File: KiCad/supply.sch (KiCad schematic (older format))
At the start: 74 parts, among them IC10 AP62301Z6-7, IC12 74HC00PW, IC13 SN74LVC1G126DCKR, IC3 TPS54561, IC4 TPS7A0518PDBVT, IC8 LM3671MF-3.3, IC9 LM3671MF-3.3, T3 BSS138APW

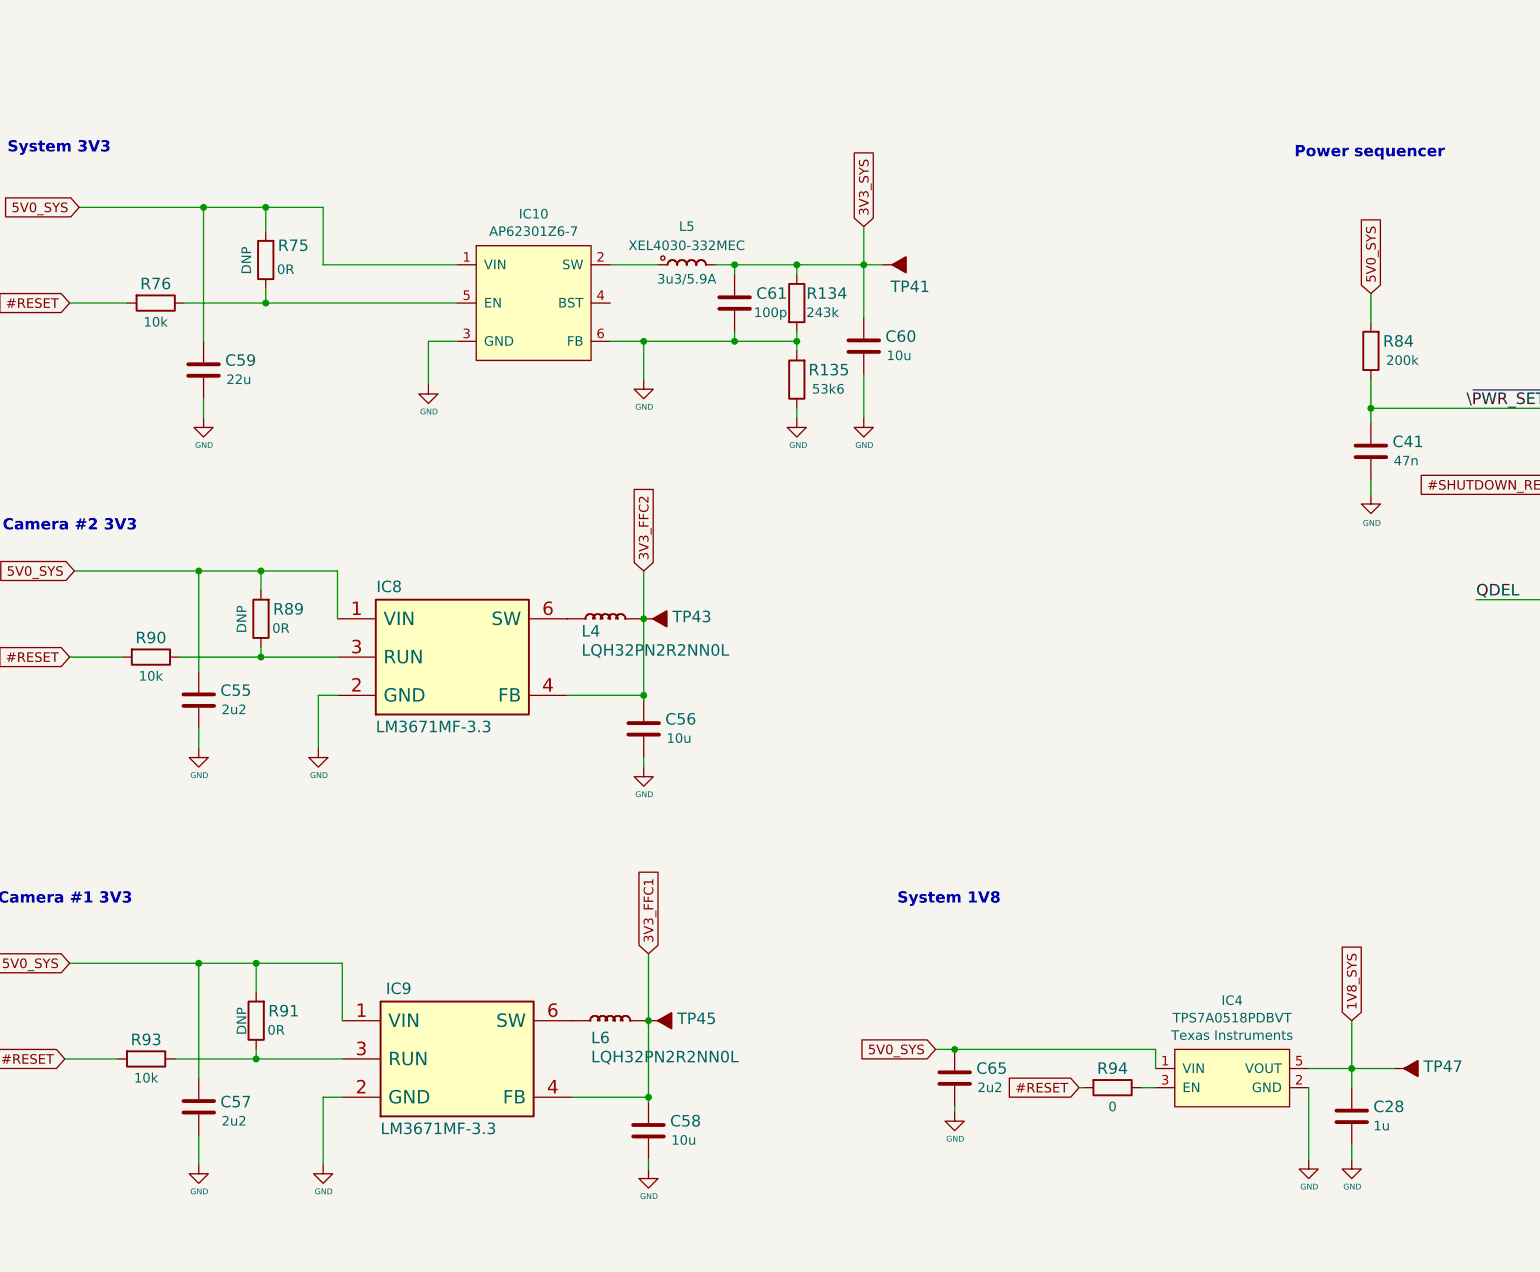
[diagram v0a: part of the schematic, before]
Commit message: DCDC passives copied
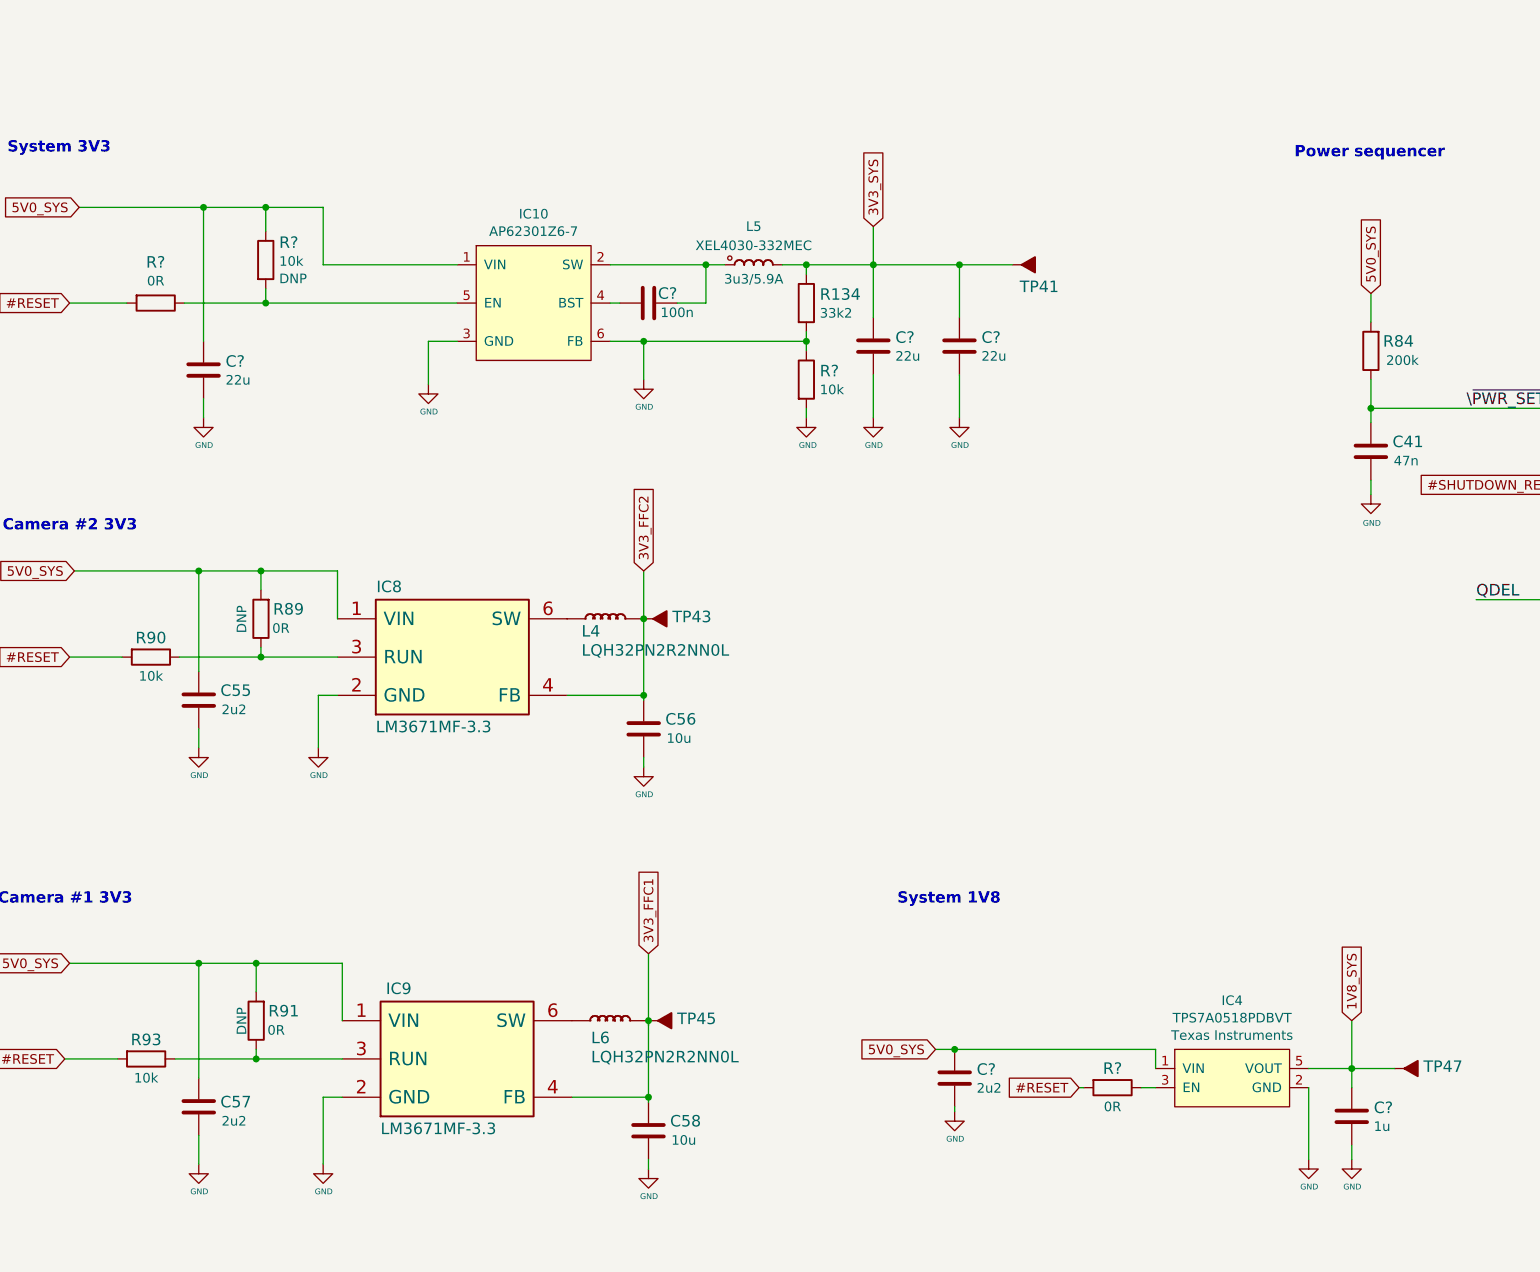
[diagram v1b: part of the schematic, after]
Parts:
- removed C28: C_1u_0402, jetson-nano-baseboard-footprints:0402-cap, symbol jetson-nano-baseboard:C_1u_0402
- removed C59: C_22u_0603, jetson-nano-baseboard-footprints:0603-cap, symbol jetson-nano-baseboard:C_2u2_0402
- removed C60: C_10u_0603, jetson-nano-baseboard-footprints:0603-cap, symbol jetson-nano-baseboard:C_10u_0603
- removed C61: C_100n_0402, jetson-nano-baseboard-footprints:0402-cap, symbol jetson-nano-baseboard:C_100p_0402
- removed C65: C_2u2_0402, jetson-nano-baseboard-footprints:0402-cap, symbol jetson-nano-baseboard:C_2u2_0402
- removed R134: R_243k_0402, jetson-nano-baseboard-footprints:0402-res, symbol jetson-nano-baseboard:R_243k_0402
- removed R135: R_53k6_0402, jetson-nano-baseboard-footprints:0402-res, symbol jetson-nano-baseboard:R_53k6_0402
- removed R75: R_10k_0402, jetson-nano-baseboard-footprints:0402-res, symbol jetson-nano-baseboard:R_0R_0402
- removed R76, R94: R_0R_0402, jetson-nano-baseboard-footprints:0402-res, symbol jetson-nano-baseboard:R_10k_0402
- added C? (x3): C_22u_0603, antmicro-footprints:0603-cap, symbol antmicroCapacitors0603:C_22u_0603
- added C?: C_100n_0402, antmicro-footprints:0402-cap, symbol antmicroCapacitors0402:C_100n_0402
- added C?: C_2u2_0402, antmicro-footprints:0402-cap, symbol antmicroCapacitors0402:C_2u2_0402
- added C?: C_1u_0402, antmicro-footprints:0402-cap, symbol antmicroCapacitors0402:C_1u_0402
- added R134: R_33k2_0402, antmicro-footprints:0402-res, symbol antmicroResistors0402:R_33k2_0402
- added R? (x2): R_10k_0402, antmicro-footprints:0402-res, symbol antmicroResistors0402:R_10k_0402
- added R? (x2): R_0R_0402, antmicro-footprints:0402-res, symbol antmicroResistors0402:R_0R_0402
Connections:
- net #RESET: now also R?.2, R?.2
- net 1V8_SYS: now also C?.1
- net 3V3_SYS: now also C?.1, C?.1, R134.1
- net 5V0_SYS: now also C?.1, C?.1, R?.1
- net GND: now also C?.2, C?.2, C?.2, C?.2, C?.2, R134.2, R?.1, R?.2
- net at IC4.3 (EN): now also R?.1
- net at IC10.2 (SW), L5.1 (P): now also C?.1
- net at IC10.4 (BST): now also C?.2
- net at IC10.5 (EN): now also R?.1, R?.2
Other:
- moved on the sheet: L5, TP41

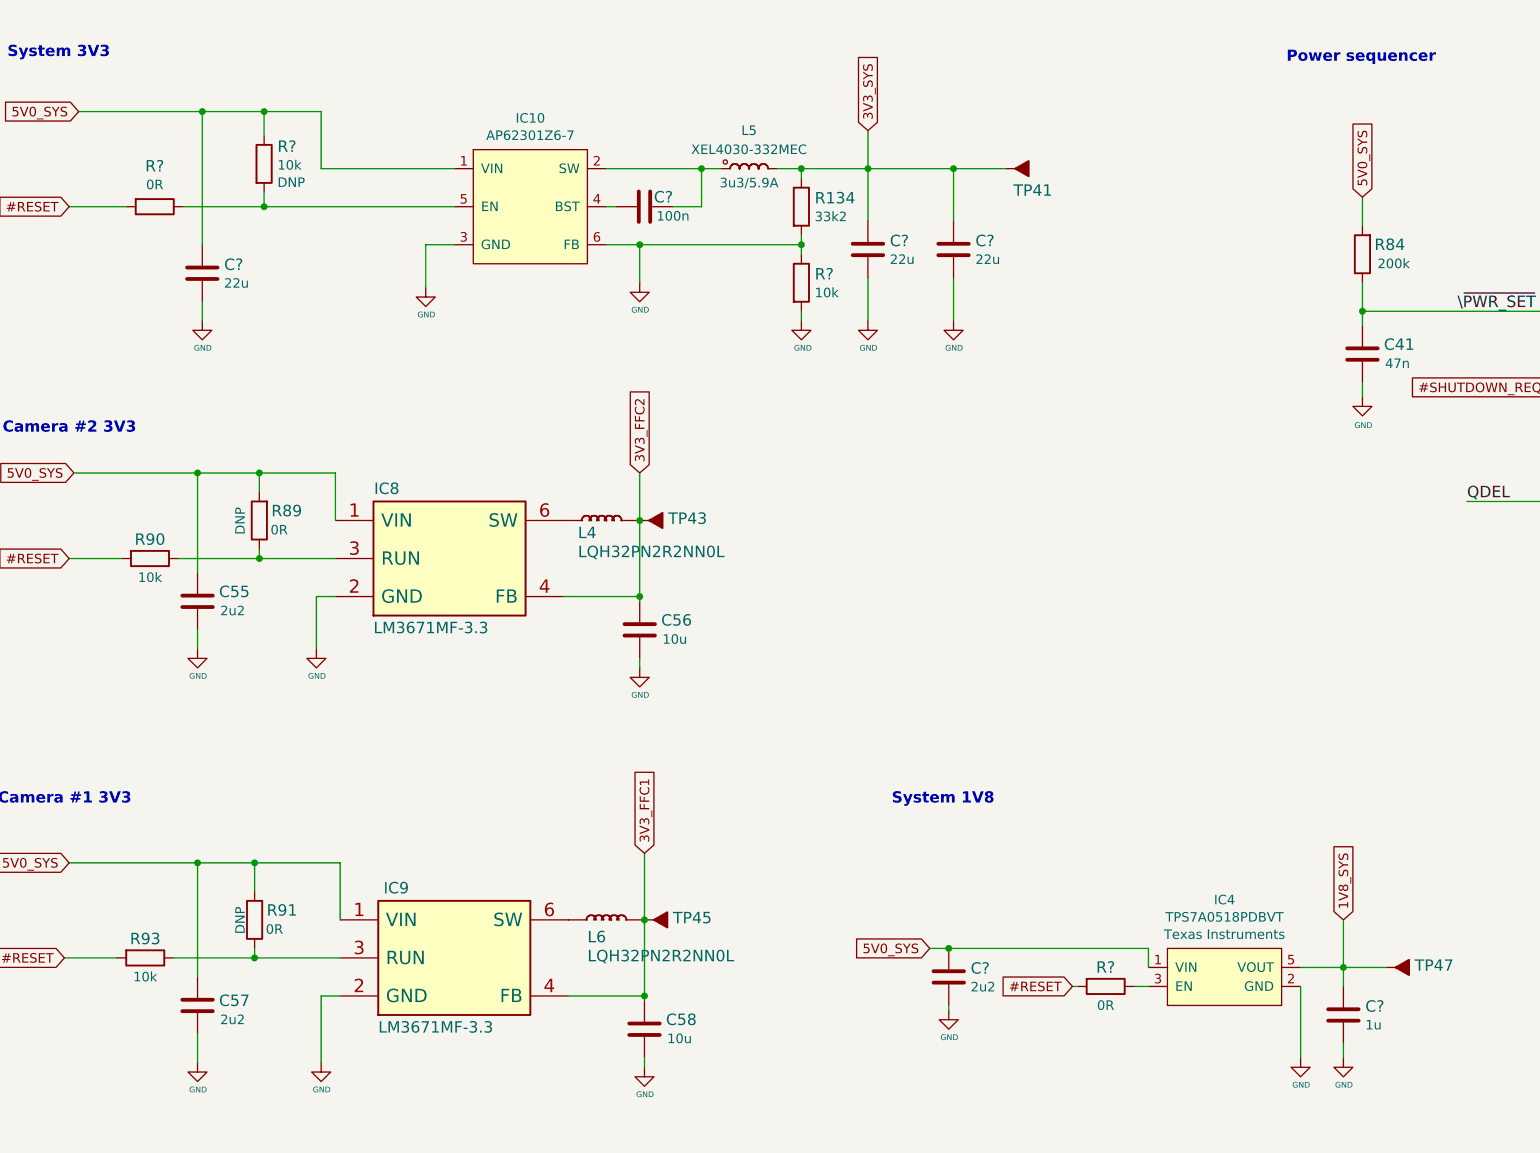
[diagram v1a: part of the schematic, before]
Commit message: Clean artefaccs, clean space for new DCDC
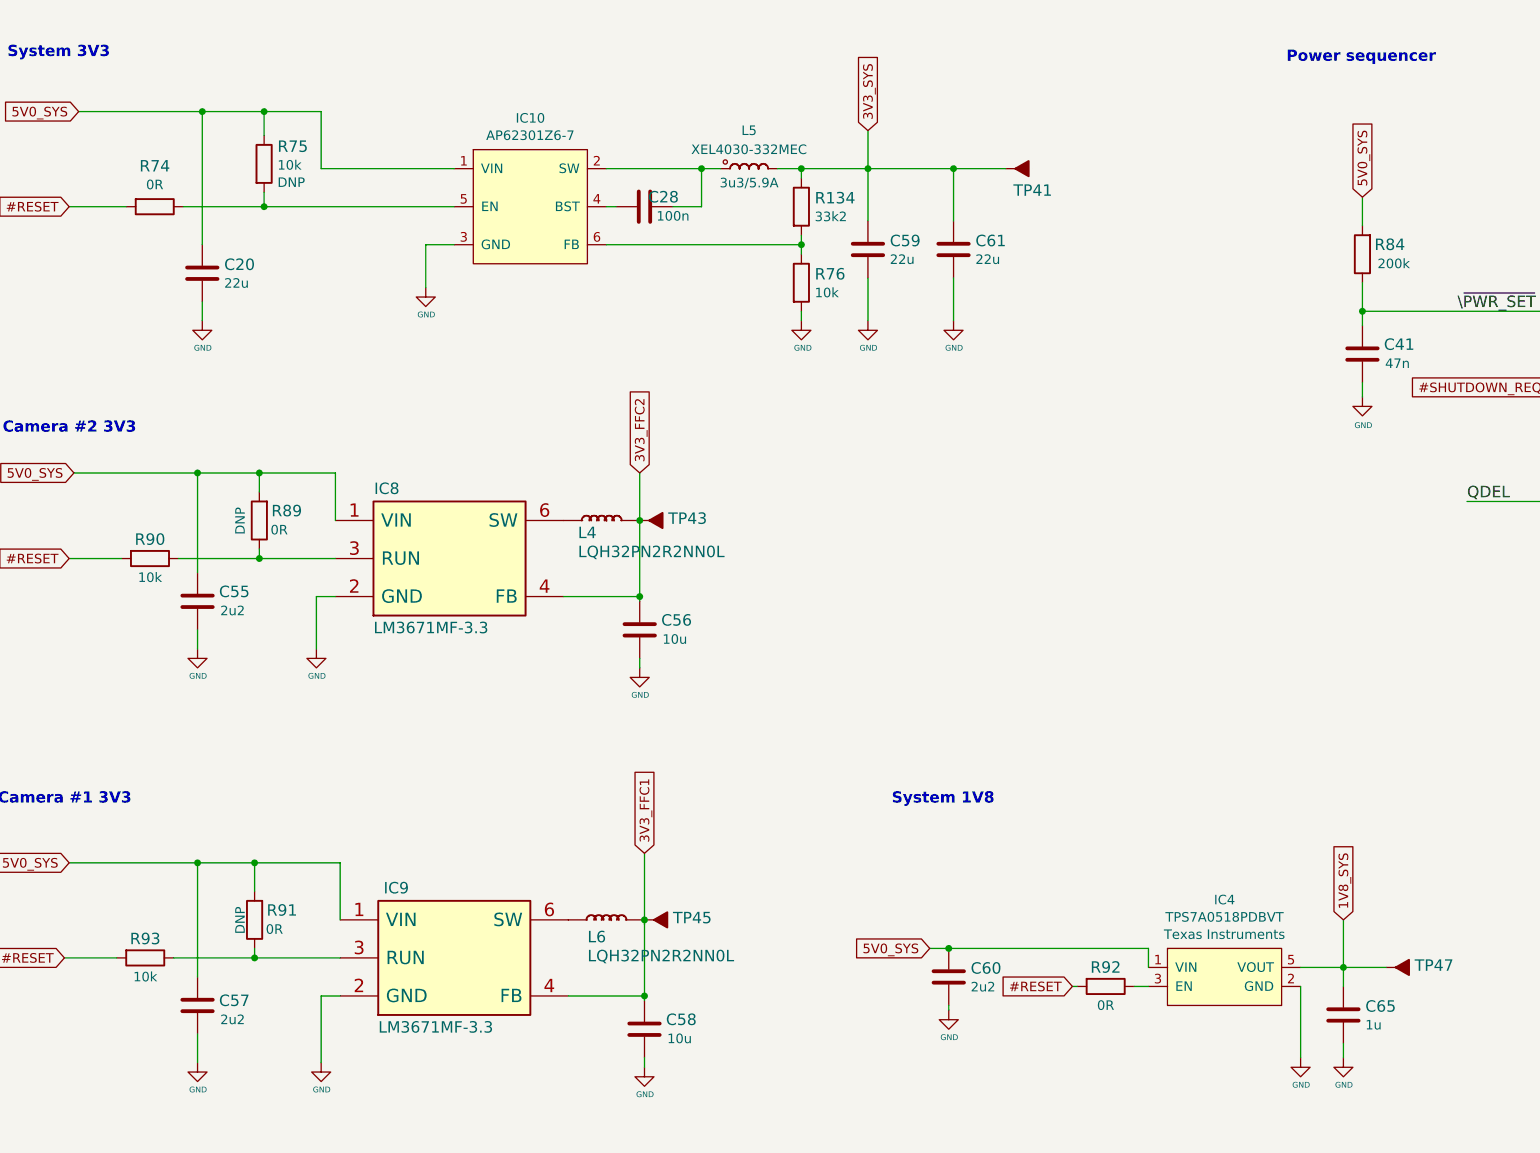
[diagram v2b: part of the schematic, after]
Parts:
- gave numbers to parts that had none: 10
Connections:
- net GND: no longer IC10.6 (FB), R134.2, R76.1
- new net: IC10.6 (FB), R134.2, R76.1
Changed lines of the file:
@@
-$EndComp
-$Comp
-L jetson-nano-baseboard:GND #GND_083
-U 1 1 5E7103BE
-P 4675 5900
-F 0 "#GND_083" H 4675 5900 20  0001 C CNN
-F 1 "GND" H 4678 5757 30  0000 C CNN
-F 2 "" H 4675 5900 70  0001 C CNN
-F 3 "" H 4675 5900 70  0001 C CNN
-	1    4675 5900
-	1    0    0    -1
 $EndComp
 $Comp
@@
 Wire Wire Line
 	3550 5700 3550 5925
-Wire Wire Line
-	4500 5700 4675 5700
-Wire Wire Line
-	4675 5700 4675 5900
 Wire Wire Line
 	1700 6900 2350 6900
@@
 $EndComp
 $Comp
-L antmicroResistors0402:R_10k_0402 R?
+L antmicroResistors0402:R_10k_0402 R76
 U 1 1 61619A9D
 P 5525 5900
-F 0 "R?" V 5480 5970 60  0000 L CNN
+F 0 "R76" V 5480 5970 60  0000 L CNN
 F 1 "R_10k_0402" H 5525 5750 60  0001 C CNN
 F 2 "antmicro-footprints:0402-res" H 5725 6100 60  0001 L CNN
@@
 $EndComp
 $Comp
-L antmicroCapacitors0603:C_22u_0603 C?
+L antmicroCapacitors0603:C_22u_0603 C59
 U 1 1 6162D00E
 P 5875 5725
-F 0 "C?" H 5990 5770 60  0000 L CNN
+F 0 "C59" H 5990 5770 60  0000 L CNN
 F 1 "C_22u_0603" H 5875 5575 60  0001 C CNN
 F 2 "antmicro-footprints:0603-cap" H 6075 5925 60  0001 L CNN
@@
 $EndComp
 $Comp
-L antmicroCapacitors0603:C_22u_0603 C?
+L antmicroCapacitors0603:C_22u_0603 C61
 U 1 1 61630270
 P 6325 5725
-F 0 "C?" H 6440 5770 60  0000 L CNN
+F 0 "C61" H 6440 5770 60  0000 L CNN
 F 1 "C_22u_0603" H 6325 5575 60  0001 C CNN
 F 2 "antmicro-footprints:0603-cap" H 6525 5925 60  0001 L CNN
@@
 $EndComp
 $Comp
-L antmicroCapacitors0402:C_100n_0402 C?
+L antmicroCapacitors0402:C_100n_0402 C28
 U 1 1 61632F02
 P 4700 5500
-F 0 "C?" V 4650 5600 60  0000 C CNN
+F 0 "C28" V 4650 5600 60  0000 C CNN
 F 1 "C_100n_0402" H 4700 5350 60  0001 C CNN
 F 2 "antmicro-footprints:0402-cap" H 4900 5700 60  0001 L CNN
@@
 $EndComp
 $Comp
-L antmicroResistors0402:R_0R_0402 R?
+L antmicroResistors0402:R_0R_0402 R74
 U 1 1 616348AD
 P 2125 5500
-F 0 "R?" H 2125 5287 60  0000 C CNN
+F 0 "R74" H 2125 5287 60  0000 C CNN
 F 1 "R_0R_0402" H 2125 5350 60  0001 C CNN
 F 2 "antmicro-footprints:0402-res" H 2325 5700 60  0001 L CNN
@@
 $EndComp
 $Comp
-L antmicroResistors0402:R_10k_0402 R?
+L antmicroResistors0402:R_10k_0402 R75
 U 1 1 61637618
 P 2700 5275
-F 0 "R?" V 2609 5345 60  0000 L CNN
+F 0 "R75" V 2609 5345 60  0000 L CNN
 F 1 "R_10k_0402" H 2700 5125 60  0001 C CNN
 F 2 "antmicro-footprints:0402-res" H 2900 5475 60  0001 L CNN
@@
 $EndComp
 $Comp
-L antmicroCapacitors0603:C_22u_0603 C?
+L antmicroCapacitors0603:C_22u_0603 C20
 U 1 1 6164BD87
 P 2375 5850
-F 0 "C?" H 2490 5895 60  0000 L CNN
+F 0 "C20" H 2490 5895 60  0000 L CNN
 F 1 "C_22u_0603" H 2375 5700 60  0001 C CNN
 F 2 "antmicro-footprints:0603-cap" H 2575 6050 60  0001 L CNN
@@
 	6325 5875 6325 6100
 $Comp
-L jetson-nano-baseboard:GND #GND_?
+L jetson-nano-baseboard:GND #GND_0151
 U 1 1 61696C07
 P 6325 6100
-F 0 "#GND_?" H 6325 6100 20  0001 C CNN
+F 0 "#GND_0151" H 6325 6100 20  0001 C CNN
 F 1 "GND" H 6328 5957 30  0000 C CNN
 F 2 "" H 6325 6100 70  0001 C CNN
@@
 Wire Wire Line
 	4500 5300 5000 5300
-Connection ~ 4675 5700
 Wire Wire Line
 	4550 5500 4500 5500
@@
 	5400 5300 5525 5300
 Wire Wire Line
-	4675 5700 5525 5700
-Wire Wire Line
 	6200 9400 6300 9400
 $Comp
-L antmicroCapacitors0402:C_2u2_0402 C?
+L antmicroCapacitors0402:C_2u2_0402 C60
 U 1 1 6173ABED
 P 6300 9550
-F 0 "C?" H 6415 9595 60  0000 L CNN
+F 0 "C60" H 6415 9595 60  0000 L CNN
 F 1 "C_2u2_0402" H 6300 9400 60  0001 C CNN
 F 2 "antmicro-footprints:0402-cap" H 6500 9750 60  0001 L CNN
@@
 	6300 9400 7350 9400
 $Comp
-L antmicroResistors0402:R_0R_0402 R?
+L antmicroResistors0402:R_0R_0402 R92
 U 1 1 6173BBE4
 P 7125 9600
-F 0 "R?" H 7125 9500 60  0000 C CNN
+F 0 "R92" H 7125 9500 60  0000 C CNN
 F 1 "R_0R_0402" H 7125 9450 60  0001 C CNN
 F 2 "antmicro-footprints:0402-res" H 7325 9800 60  0001 L CNN
@@
 $EndComp
 $Comp
-L antmicroCapacitors0402:C_1u_0402 C?
+L antmicroCapacitors0402:C_1u_0402 C65
 U 1 1 6173EACE
 P 8375 9750
-F 0 "C?" H 8490 9795 60  0000 L CNN
+F 0 "C65" H 8490 9795 60  0000 L CNN
 F 1 "C_1u_0402" H 8375 9600 60  0001 C CNN
 F 2 "antmicro-footprints:0402-cap" H 8575 9950 60  0001 L CNN
@@
 	1    0    0    -1
 $EndComp
+Wire Wire Line
+	4500 5700 5525 5700
 $EndSCHEMATC
